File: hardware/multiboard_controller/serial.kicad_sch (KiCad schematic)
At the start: 0 parts

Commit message: Adding USB Connector for Power and Data
First USB connector is for power and data input from the host. Power is taken from the V_BUS line and stepped to 3V3 to power other components using an LDO. Updated block diagram accordingly.
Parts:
- added U2: TUSB3410RHBR, RHB32_3P45X3P45, symbol 2025-02-09_21-04-15:TUSB3410RHBR
- added U3: FT232RL, Package_SO:SSOP-28_5.3x10.2mm_P0.65mm, symbol Interface_USB:FT232RL
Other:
- note added: "USB-to-Serial Convertor"

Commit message: Add Channel Select switches and USB output ports
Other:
- title: (none) -> Serial Conversion
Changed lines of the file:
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@@
 	(generator_version "8.0")
 	(paper "A4")
+	(title_block
+		(title "Serial Conversion")
+	)
 	(text "USB-to-Serial Convertor"
 		(exclude_from_sim no)

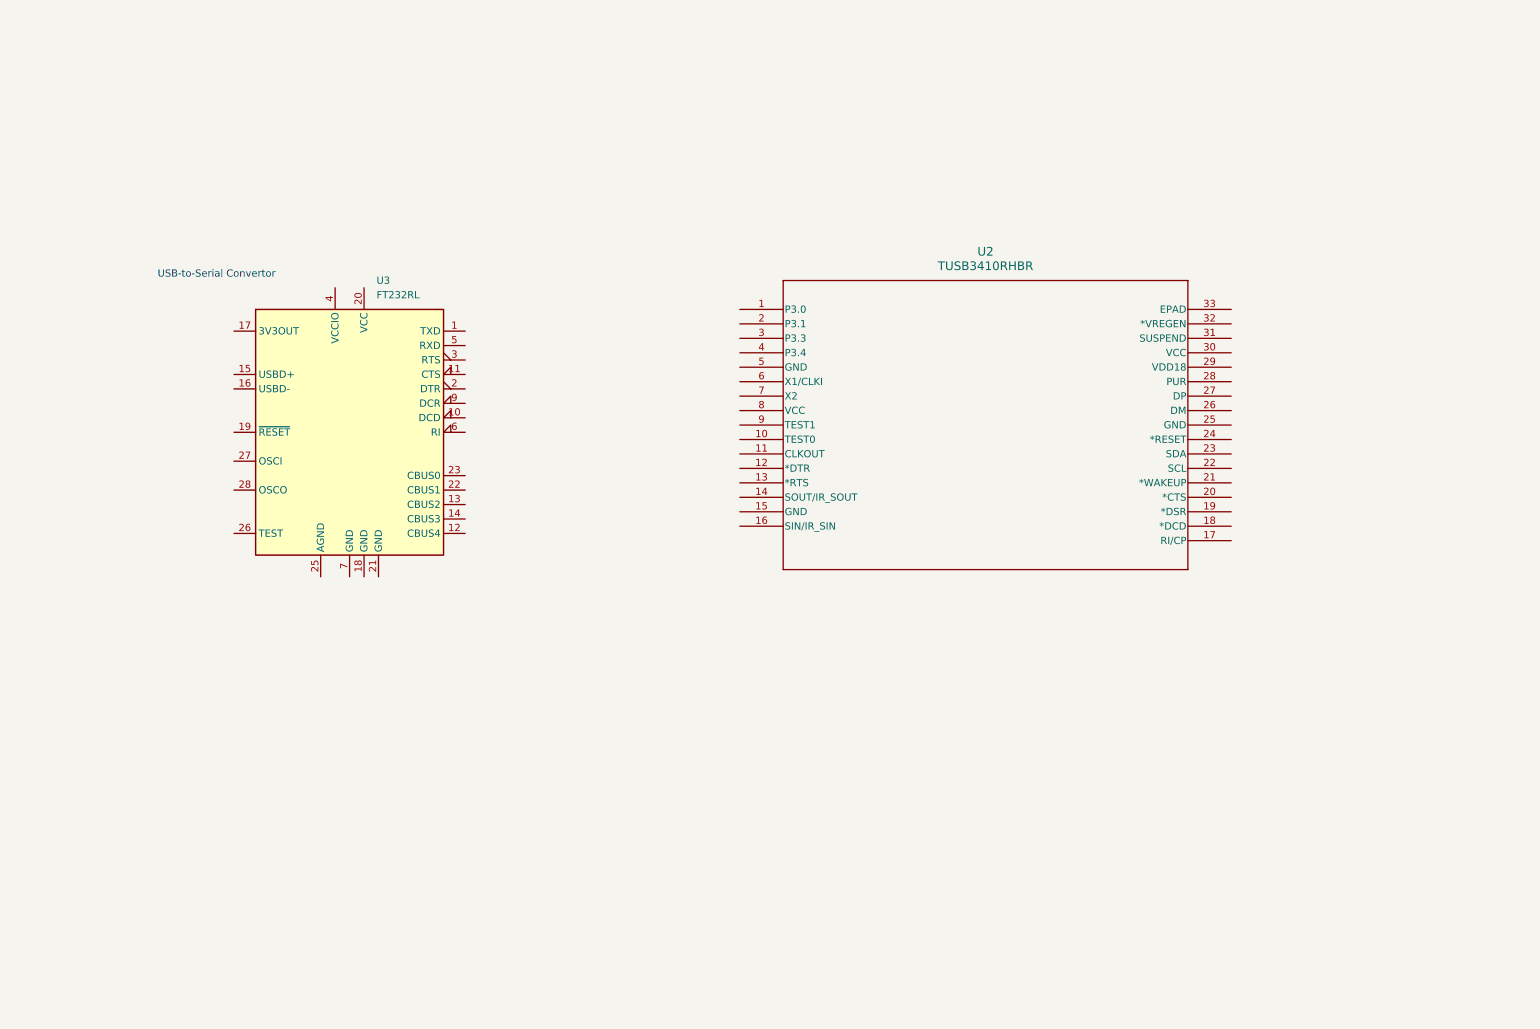
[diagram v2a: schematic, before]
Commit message: Choose switches for UART muxing. USB-to-UART schematic WIP.
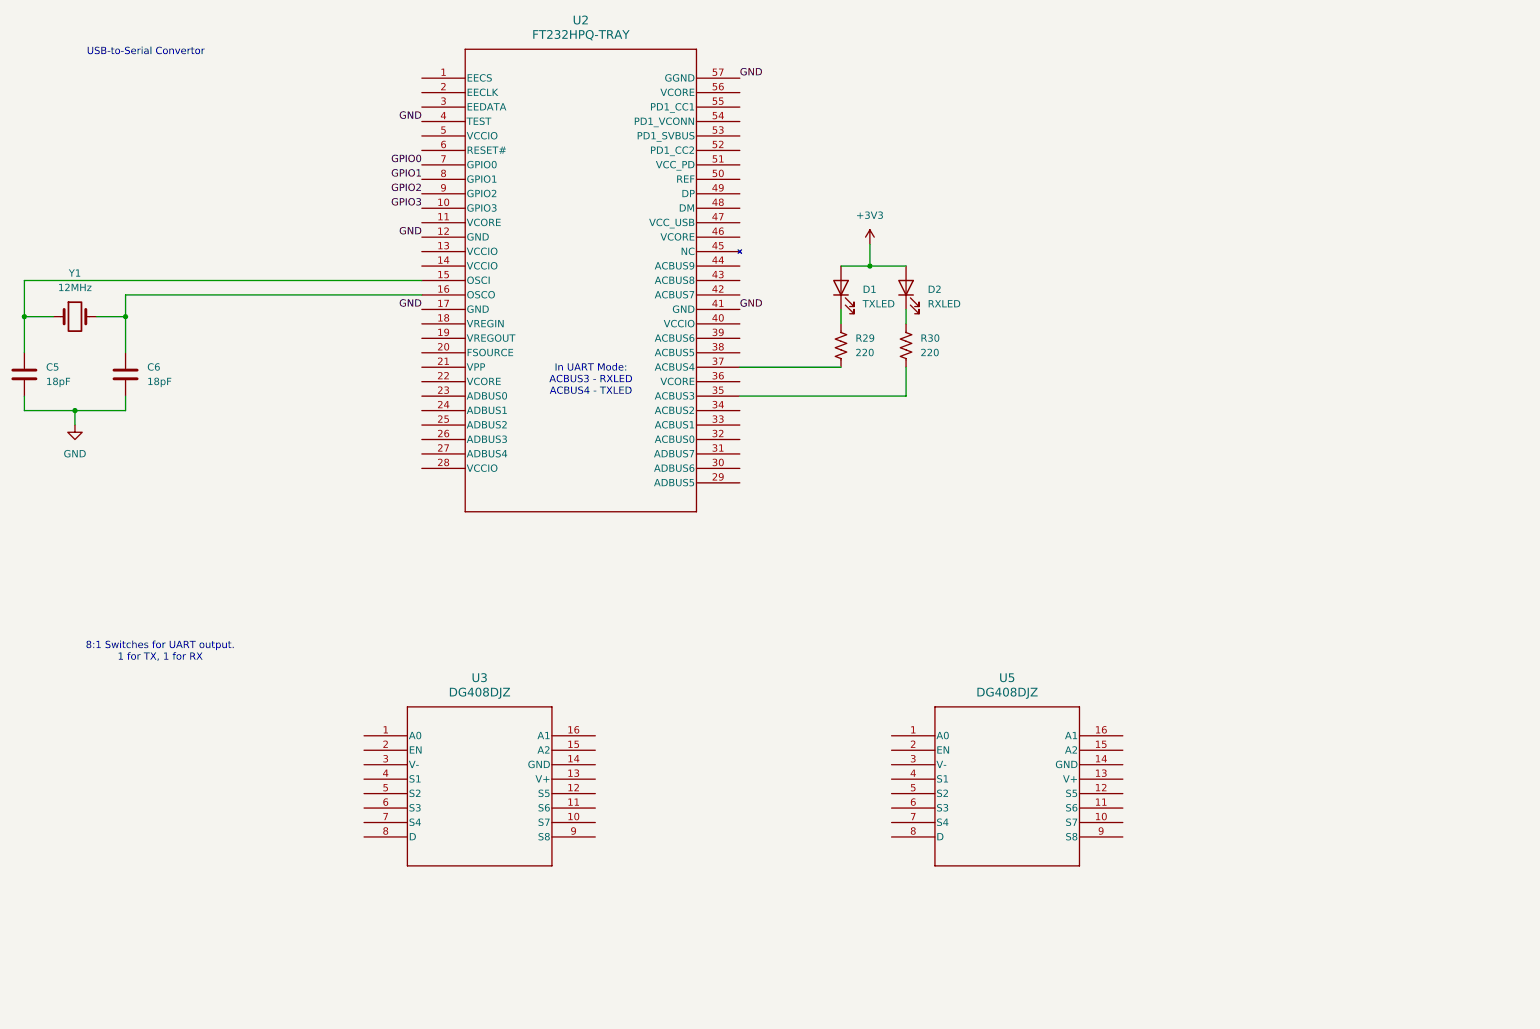
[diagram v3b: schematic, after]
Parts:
- removed U2: TUSB3410RHBR, RHB32_3P45X3P45, symbol 2025-02-09_21-04-15:TUSB3410RHBR
- removed U3: FT232RL, Package_SO:SSOP-28_5.3x10.2mm_P0.65mm, symbol Interface_USB:FT232RL
- added C5, C6: 18pF, symbol Device:C
- added D1: TXLED, symbol Device:LED
- added D2: RXLED, symbol Device:LED
- added R29, R30: 220, symbol Device:R_US
- added U2: FT232HPQ-TRAY, QFN-56_FT232HPQ_FTD, symbol 2025-02-15_17-50-50:FT232HPQ-TRAY
- added U3, U5: DG408DJZ, PDIP16_E16.3_REN, symbol 2025-02-15_19-41-54:DG408DJZ
- added Y1: 12MHz, symbol Device:Crystal
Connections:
- new net: D1.1 (K), R29.1
- new net: R29.2, U2.37 (ACBUS4)
- new net: D2.1 (K), R30.1
- new net: R30.2, U2.35 (ACBUS3)
- new net: C5.1, U2.15 (OSCI), Y1.1
- new net: C6.1, U2.16 (OSCO), Y1.2
- new net +3V3: D1.2 (A), D2.2 (A)
- new net GND: C5.2, C6.2, U2.12 (GND), U2.17 (GND), U2.4 (TEST), U2.41 (GND), U2.57 (GGND)
- new net GPIO0: U2.7 (GPIO0)
- new net GPIO1: U2.8 (GPIO1)
- new net GPIO2: U2.9 (GPIO2)
- new net GPIO3: U2.10 (GPIO3)
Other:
- note added: "8:1 Switches for UART output. 1 for TX, 1 for RX"
- note added: "In UART Mode: ACBUS3 - RXLED ACBUS4 - TXLED"

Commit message: Connecting first UART line out from mux
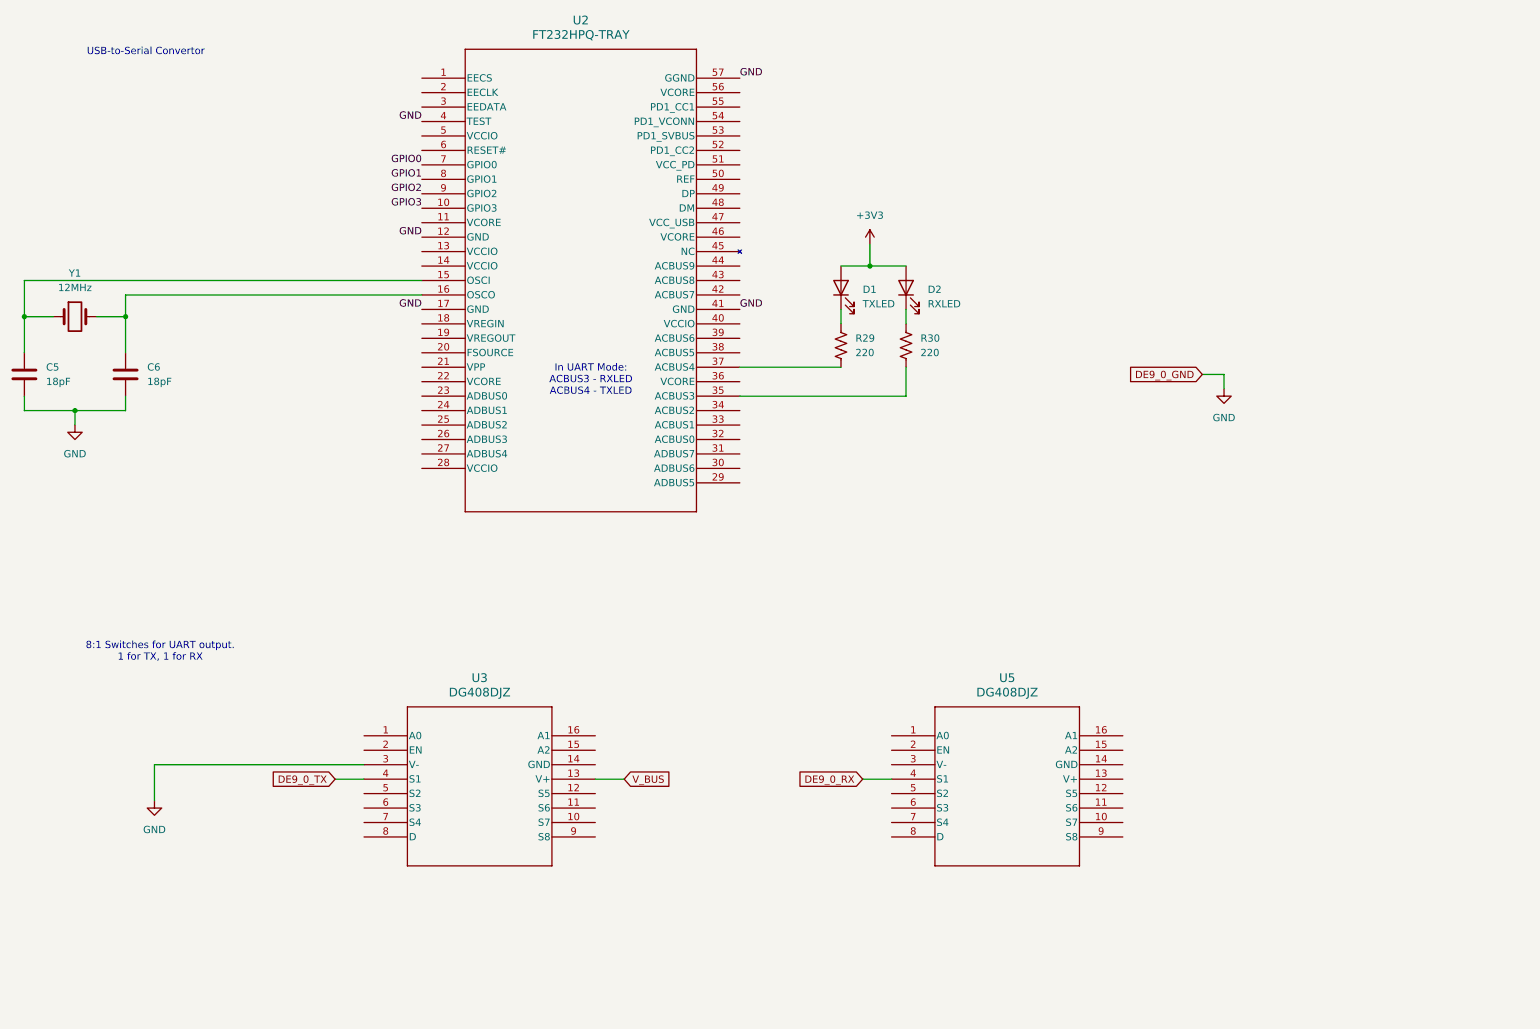
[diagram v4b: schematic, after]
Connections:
- net GND: now also U3.3 (V-)
- net DE9_0_RX: now reaches U5.4 (S1)
- net V_BUS: now reaches U3.13 (V+)
- net DE9_0_TX: now reaches U3.4 (S1)

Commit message: Full USB-to-UART connections
- Connect switches and convertor IC in USB-UART mode
- Change CH_EN input signal from momentary button to switch to work with
  switch chips (since it expects high enable to output signal)

TODOs:
- Confirm that resistors built into ICs are enough to protect USB/UART
  signals.
- Rework select circuitry to automatically enable after certain time
  period (but without adding ucontroller) -- possibly using caps or 555?
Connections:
- net +3V3: now also U2.13 (VCCIO), U2.14 (VCCIO), U2.18 (VREGIN), U2.28 (VCCIO), U2.40 (VCCIO), U2.5 (VCCIO)
- net GND: now also U3.14 (GND), U5.14 (GND), U5.3 (V-)
- net V_BUS: now also U5.13 (V+)
- net C0: now reaches U5.1 (A0)
- net C0: now also U3.1 (A0)
- net DE9_6_RX: now reaches U5.10 (S7)
- net DE9_5_RX: now reaches U5.11 (S6)
- net DE9_4_RX: now reaches U5.12 (S5)
- net C2: now reaches U5.15 (A2)
- net C2: now also U3.15 (A2)
- net C1: now reaches U5.16 (A1)
- net C1: now also U3.16 (A1)
- net CH_EN: now reaches U5.2 (EN)
- net CH_EN: now also U3.2 (EN)
- net DE9_1_RX: now reaches U5.5 (S2)
- net DE9_2_RX: now reaches U5.6 (S3)
- net DE9_3_RX: now reaches U5.7 (S4)
- net RXD: now reaches U5.8 (D)
- net RXD: now also U2.24 (ADBUS1)
- net DE9_7_RX: now reaches U5.9 (S8)
- net VREGOUT: now reaches U2.11 (VCORE)
- net VREGOUT: now also U2.19 (VREGOUT), U2.22 (VCORE), U2.36 (VCORE), U2.46 (VCORE), U2.56 (VCORE)
- net TXD: now reaches U2.23 (ADBUS0)
- net TXD: now also U3.8 (D)
- net RTS: now reaches U2.25 (ADBUS2)
- net CTS: now reaches U2.26 (ADBUS3)
- net DTR: now reaches U2.27 (ADBUS4)
- net DSR: now reaches U2.29 (ADBUS5)
- net DCD: now reaches U2.30 (ADBUS6)
- net RI: now reaches U2.31 (ADBUS7)
- net DE9_6_TX: now reaches U3.10 (S7)
- net DE9_5_TX: now reaches U3.11 (S6)
- net DE9_4_TX: now reaches U3.12 (S5)
- net DE9_1_TX: now reaches U3.5 (S2)
- net DE9_2_TX: now reaches U3.6 (S3)
- net DE9_3_TX: now reaches U3.7 (S4)
- net DE9_7_TX: now reaches U3.9 (S8)
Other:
- note added: "All DE9 GND pins connect to global GND"
- note added: "GPIO for bitbang mode (not needed)"
- note added: "USB Input"
- note added: "https://www.mouser.com/datasheet/2/163/DS_FT233HP-3555364.pdf"
